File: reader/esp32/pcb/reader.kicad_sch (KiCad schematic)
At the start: 25 parts, among them J2 RS485, J4 Debug, Q1 MMBT3904, Q2 MMBT3904, U1 ESP32-WROOM-32U, U3 MAX485E, U5 AMS1117-3.3, U5 RDM6300

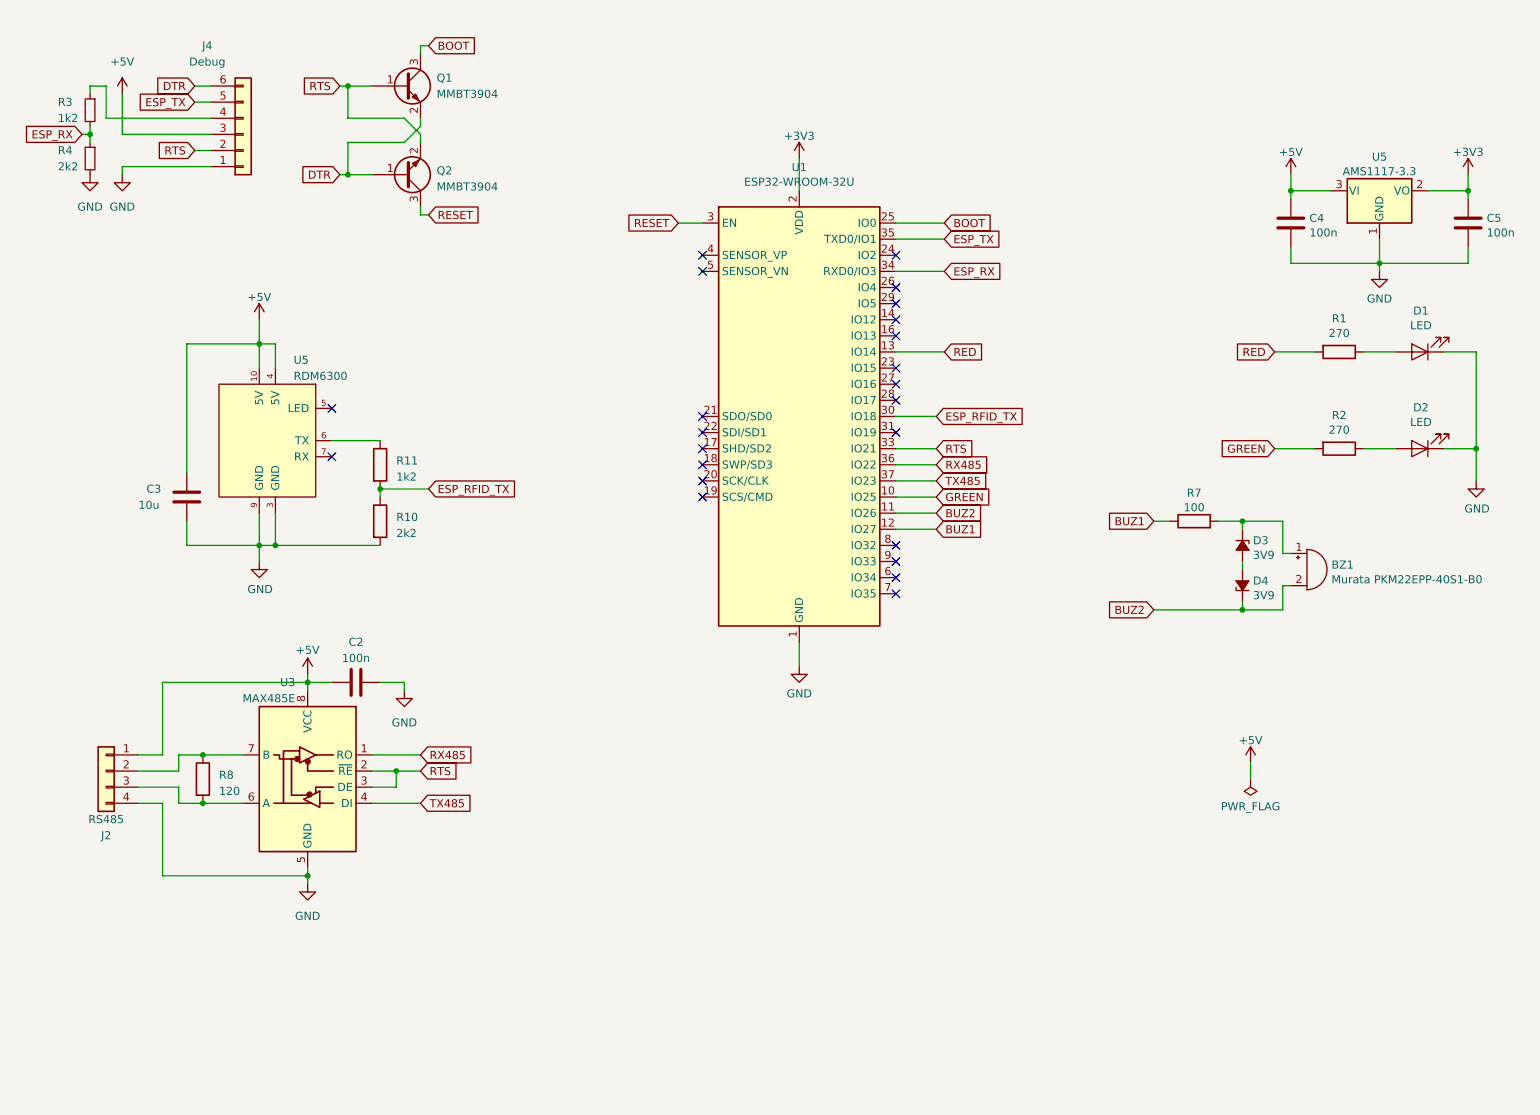
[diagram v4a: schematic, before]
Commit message: Change to WROOM32U.
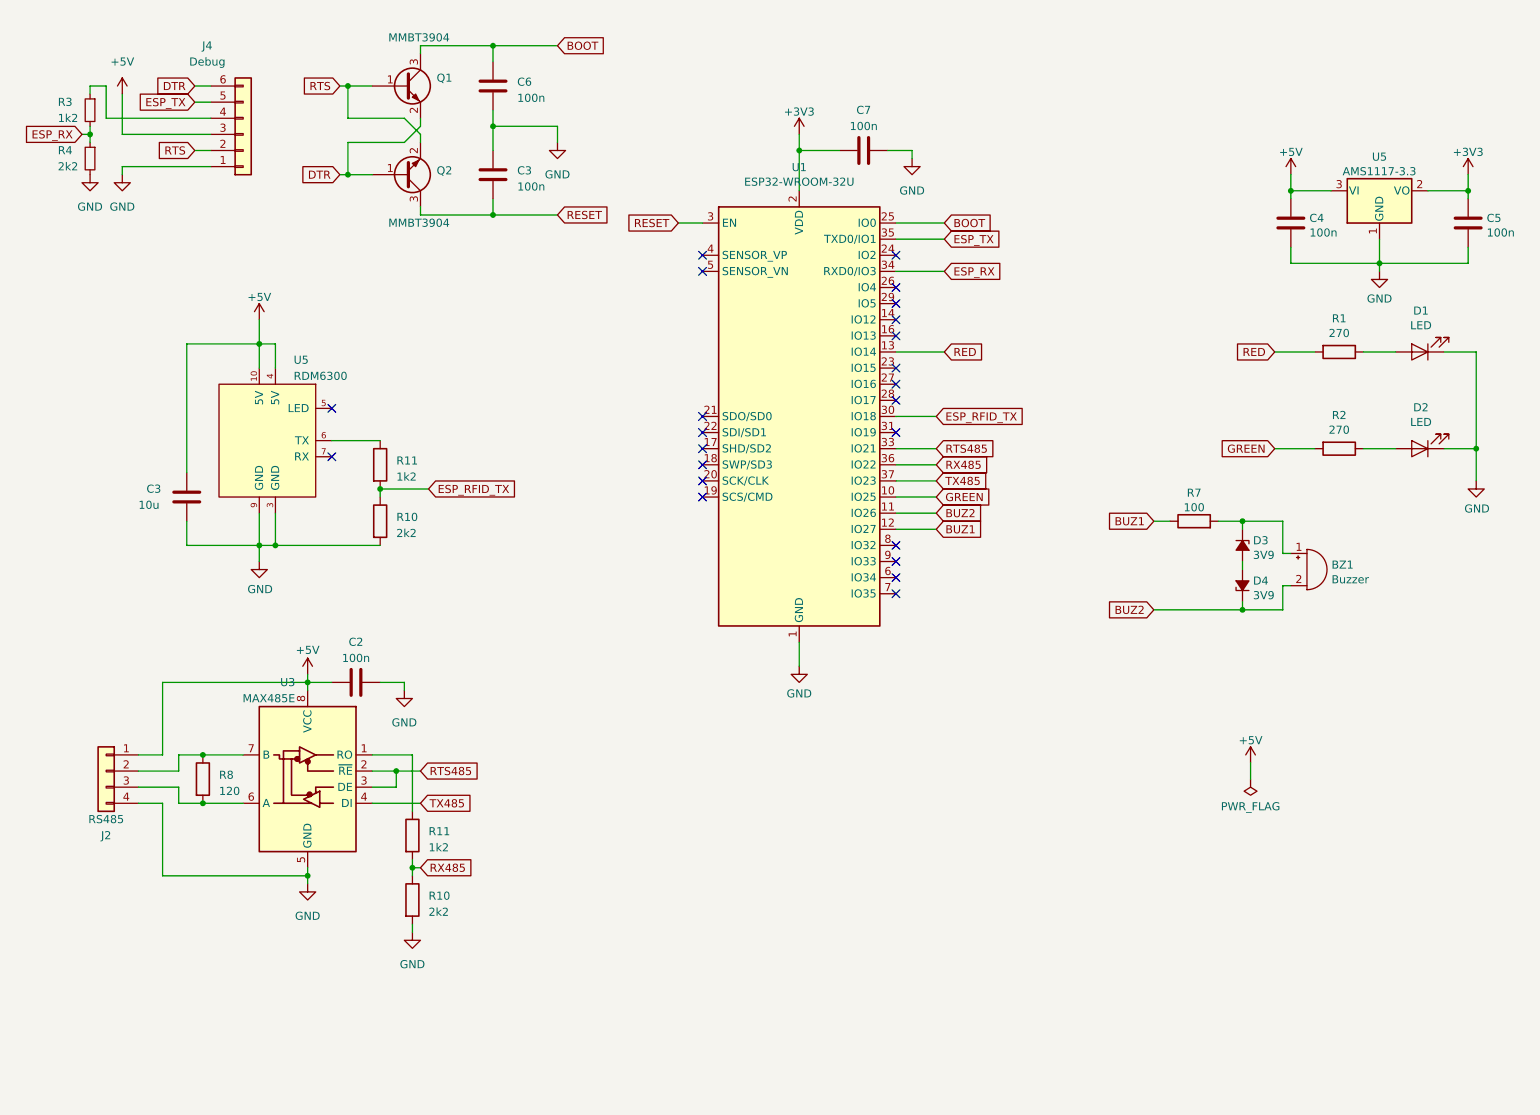
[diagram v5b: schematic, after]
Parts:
- added C3, C6, C7: 100n, Capacitor_SMD:C_0603_1608Metric, symbol Device:C
- added R10: 2k2, Resistor_SMD:R_0603_1608Metric, symbol Device:R
- added R11: 1k2, Resistor_SMD:R_0603_1608Metric, symbol Device:R
- BZ1: value Murata PKM22EPP-40S1-B0 -> Buzzer; footprint Module:Buzzer_D14mm_H7mm_P7.62mm -> Module:Buzzer_D22mm_H8mm_P10mm
- U1: footprint RF_Module:ESP32-WROOM-32 -> RF_Module:ESP32-WROOM-32U
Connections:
- net +3V3: now also C7.1
- net BOOT: now also C6.1
- net GND: now also C3.1, C6.2, C7.2, R10.2
- net RESET: now also C3.2
- net RTS: no longer U1.33 (IO21), U3.2 (~{RE}), U3.3 (DE)
- net RX485: now also R10.1, R11.2; no longer U3.1 (RO)
- new net: R11.1, U3.1 (RO)
- new net RTS485: U1.33 (IO21), U3.2 (~{RE}), U3.3 (DE)

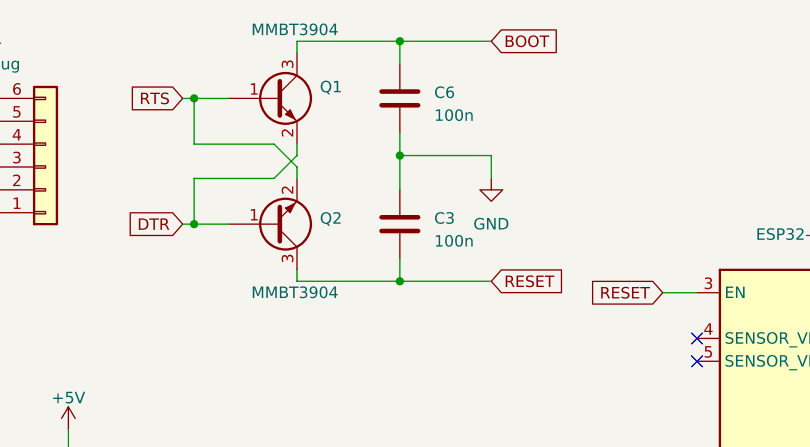
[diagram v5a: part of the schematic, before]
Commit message: Remove capacitors.
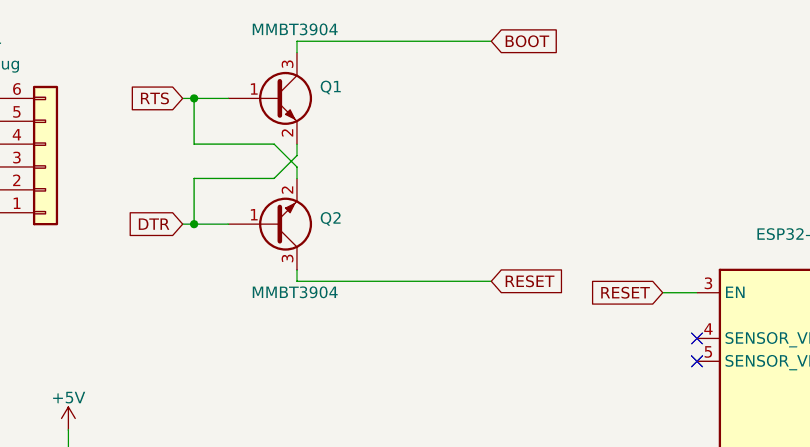
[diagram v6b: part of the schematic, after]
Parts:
- removed C3, C6: 100n, Capacitor_SMD:C_0603_1608Metric, symbol Device:C
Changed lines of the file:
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@@
   (junction (at 247.65 45.72) (diameter 0) (color 0 0 0 0)
   )
-  (junction (at 93.98 22.86) (diameter 0) (color 0 0 0 0)
-  )
   (junction (at 142.24 39.37) (diameter 0) (color 0 0 0 0)
   )
-  (junction (at 93.98 49.53) (diameter 0) (color 0 0 0 0)
-  )
   (junction (at 78.74 137.16) (diameter 0) (color 0 0 0 0)
-  )
-  (junction (at 93.98 35.56) (diameter 0) (color 0 0 0 0)
   )
   (junction (at 233.68 57.15) (diameter 0) (color 0 0 0 0)
@@
     (stroke (width 0) (type default))
   )
-  (wire (pts (xy 93.98 35.56) (xy 93.98 39.37))
-    (stroke (width 0) (type default))
-  )
   (wire (pts (xy 57.15 96.52) (xy 57.15 101.6))
     (stroke (width 0) (type default))
@@
   )
   (wire (pts (xy 35.56 36.83) (xy 49.53 36.83))
-    (stroke (width 0) (type default))
-  )
-  (wire (pts (xy 93.98 22.86) (xy 93.98 25.4))
     (stroke (width 0) (type default))
   )
@@
     (stroke (width 0) (type default))
   )
-  (wire (pts (xy 93.98 22.86) (xy 104.14 22.86))
-    (stroke (width 0) (type default))
-  )
   (wire (pts (xy 157.48 86.36) (xy 163.83 86.36))
     (stroke (width 0) (type default))
   )
   (wire (pts (xy 80.01 123.19) (xy 76.2 123.19))
-    (stroke (width 0) (type default))
-  )
-  (wire (pts (xy 93.98 49.53) (xy 104.14 49.53))
     (stroke (width 0) (type default))
   )
@@
     (stroke (width 0) (type default))
   )
-  (wire (pts (xy 82.55 22.86) (xy 93.98 22.86))
+  (wire (pts (xy 82.55 22.86) (xy 104.14 22.86))
     (stroke (width 0) (type default))
   )
@@
     (stroke (width 0) (type default))
   )
-  (wire (pts (xy 93.98 46.99) (xy 93.98 49.53))
-    (stroke (width 0) (type default))
-  )
   (wire (pts (xy 81.28 152.4) (xy 81.28 153.67))
     (stroke (width 0) (type default))
@@
     (stroke (width 0) (type default))
   )
-  (wire (pts (xy 82.55 49.53) (xy 93.98 49.53))
+  (wire (pts (xy 82.55 49.53) (xy 104.14 49.53))
     (stroke (width 0) (type default))
   )
@@
     (stroke (width 0) (type default))
   )
-  (wire (pts (xy 93.98 33.02) (xy 93.98 35.56))
-    (stroke (width 0) (type default))
-  )
   (wire (pts (xy 80.01 34.29) (xy 71.12 34.29))
     (stroke (width 0) (type default))
@@
     (stroke (width 0) (type default))
   )
-  (wire (pts (xy 104.14 35.56) (xy 93.98 35.56))
-    (stroke (width 0) (type default))
-  )
   (wire (pts (xy 45.72 69.85) (xy 45.72 90.17))
     (stroke (width 0) (type default))
@@
   )
   (wire (pts (xy 35.56 41.91) (xy 35.56 43.18))
-    (stroke (width 0) (type default))
-  )
-  (wire (pts (xy 104.14 38.1) (xy 104.14 35.56))
     (stroke (width 0) (type default))
   )
@@
     )
   )
-  (symbol (lib_name "GND_3") (lib_id "power:GND") (at 104.14 38.1 0) (unit 1)
-    (in_bom yes) (on_board yes) (dnp no) (fields_autoplaced)
-    (property "Reference" "#PWR010" (at 104.14 44.45 0)
-      (effects (font (size 1.27 1.27)) hide)
-    )
-    (property "Value" "GND" (at 104.14 43.18 0)
-      (effects (font (size 1.27 1.27)))
-    )
-    (property "Footprint" "" (at 104.14 38.1 0)
-      (effects (font (size 1.27 1.27)) hide)
-    )
-    (property "Datasheet" "" (at 104.14 38.1 0)
-      (effects (font (size 1.27 1.27)) hide)
-    )
-    (pin "1")
-    (instances
-      (project "reader"
-        (path "/218f1b12-ca06-4253-bcd5-950f07f2eb16"
-          (reference "#PWR010") (unit 1)
-        )
-      )
-    )
-  )
   (symbol (lib_id "Device:R") (at 81.28 147.32 0) (unit 1)
     (in_bom yes) (on_board yes) (dnp no) (fields_autoplaced)
@@
         )
       )
-    )
-  )
-  (symbol (lib_name "C_2") (lib_id "Device:C") (at 93.98 43.18 0) (unit 1)
-    (in_bom yes) (on_board yes) (dnp no) (fields_autoplaced)
-    (property "Reference" "C3" (at 97.79 42.545 0)
-      (effects (font (size 1.27 1.27)) (justify left))
-    )
-    (property "Value" "100n" (at 97.79 45.085 0)
-      (effects (font (size 1.27 1.27)) (justify left))
-    )
-    (property "Footprint" "Capacitor_SMD:C_0603_1608Metric" (at 94.9452 46.99 0)
-      (effects (font (size 1.27 1.27)) hide)
-    )
-    (property "Datasheet" "~" (at 93.98 43.18 0)
-      (effects (font (size 1.27 1.27)) hide)
-    )
-    (pin "1")
-    (pin "2")
-    (instances
-      (project "reader"
-        (path "/218f1b12-ca06-4253-bcd5-950f07f2eb16"
-          (reference "C3") (unit 1)
-        )
-      )
-    )
-  )
-  (symbol (lib_name "C_3") (lib_id "Device:C") (at 93.98 29.21 0) (unit 1)
-    (in_bom yes) (on_board yes) (dnp no) (fields_autoplaced)
-    (property "Reference" "C6" (at 97.79 28.575 0)
-      (effects (font (size 1.27 1.27)) (justify left))
-    )
-    (property "Value" "100n" (at 97.79 31.115 0)
-      (effects (font (size 1.27 1.27)) (justify left))
-    )
-    (property "Footprint" "Capacitor_SMD:C_0603_1608Metric" (at 94.9452 33.02 0)
-      (effects (font (size 1.27 1.27)) hide)
-    )
-    (property "Datasheet" "~" (at 93.98 29.21 0)
-      (effects (font (size 1.27 1.27)) hide)
-    )
-    (pin "1")
-    (pin "2")
-    (instances
-      (project "reader"
-        (path "/218f1b12-ca06-4253-bcd5-950f07f2eb16"
-          (reference "C6") (unit 1)
-        )
-      )

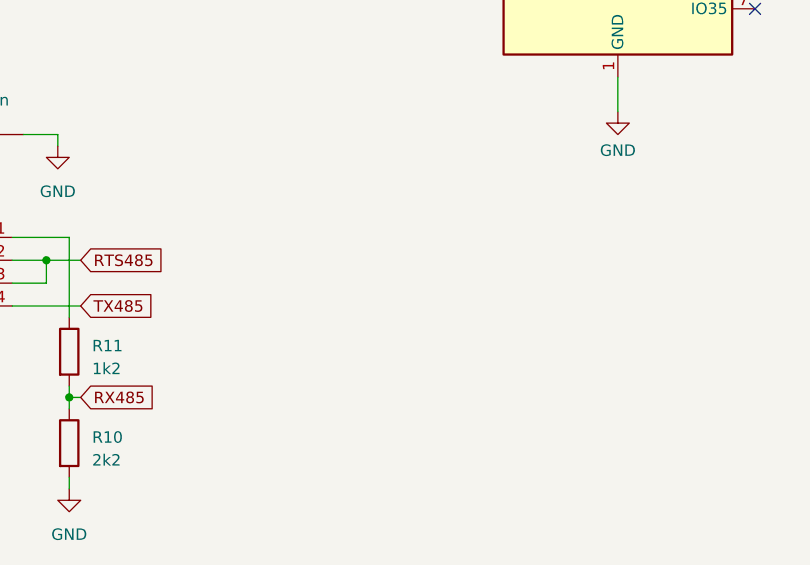
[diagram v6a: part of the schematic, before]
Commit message: Add RTS pullup; move RS485 connector.
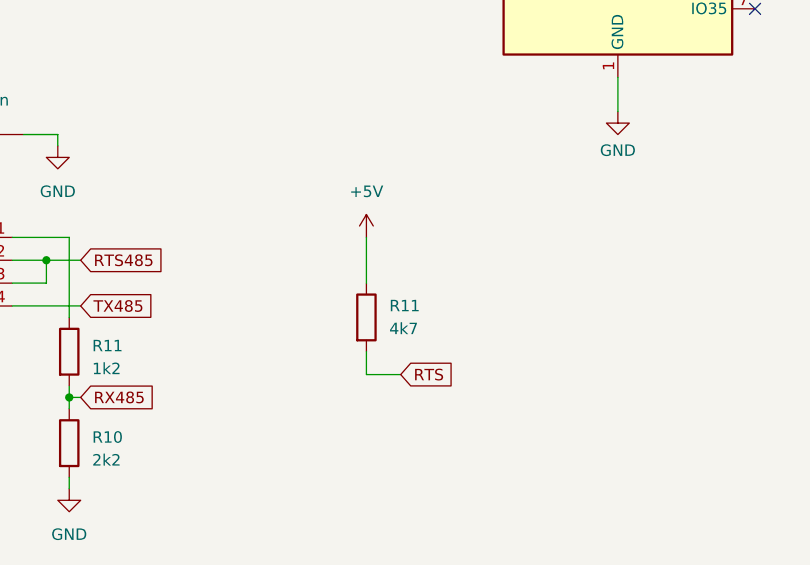
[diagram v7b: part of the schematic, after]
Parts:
- added R11: 4k7, Resistor_SMD:R_0603_1608Metric, symbol Device:R
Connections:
- net +5V: now also R11.1
- net RTS: now also R11.2
